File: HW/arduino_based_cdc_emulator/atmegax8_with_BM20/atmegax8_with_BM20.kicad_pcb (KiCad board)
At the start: 2 copper layers, 66 parts, among them IC1 ATMEGA88-A, J1 TEST_FLASH_MODE, P1 CONN_10, P2 SPI, U1 78L05-RESCUE-atmegax8_with_BM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, U2 BM20, U3 LM358, Y1 Crystal_GND24

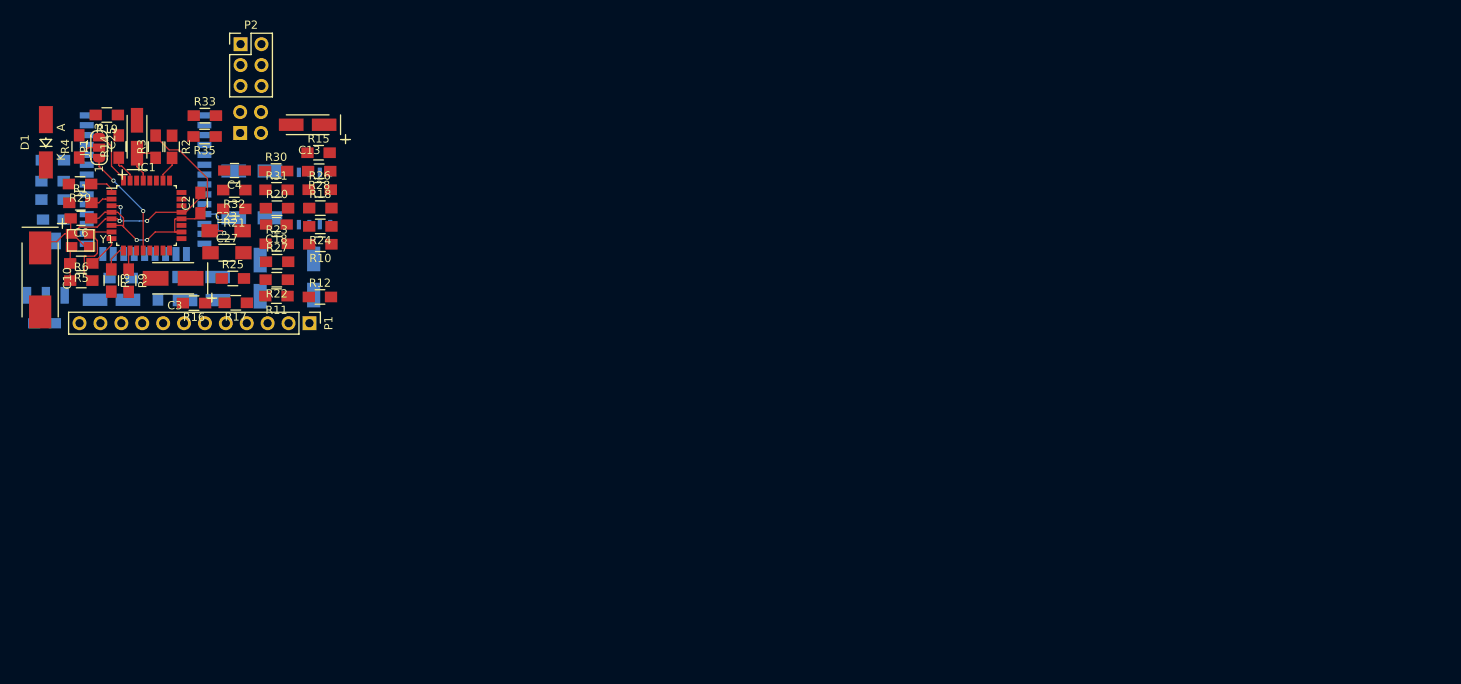
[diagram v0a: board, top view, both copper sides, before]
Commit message: bm20 version update to 328PB
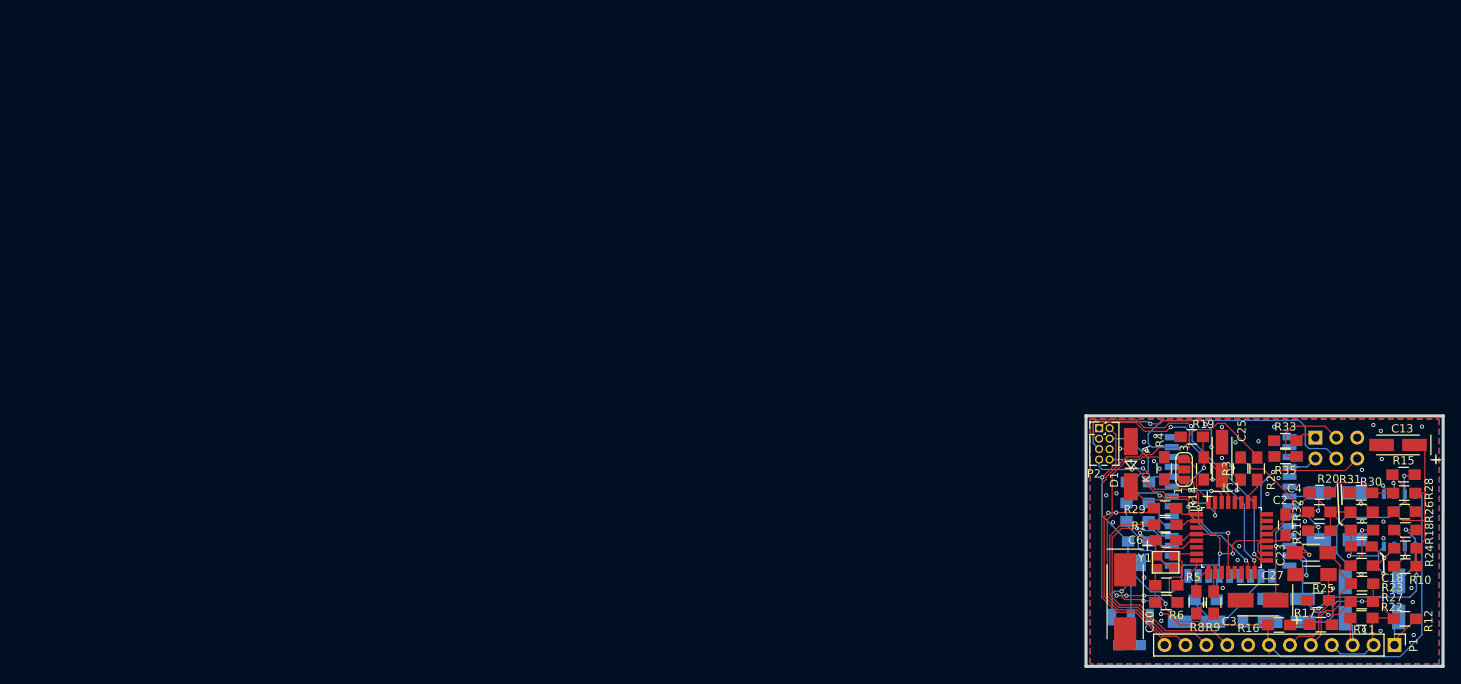
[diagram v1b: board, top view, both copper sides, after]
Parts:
- C14: value 4u7/25V -> 10u/16V
- C9: value 47m/25V -> 10m/16V
- IC1: value ATMEGA88-A -> ATMEGA328PB-AU; footprint Housings_QFP.pretty:LQFP-32_7x7mm_Pitch0.8mm -> Housings_QFP.pretty:TQFP-32_7x7mm_Pitch0.8mm
- J1: footprint Pin_Headers:Pin_Header_Straight_2x02_Pitch2.54mm -> Pin_Headers:Pin_Header_Straight_2x03_Pitch2.54mm
- P2: footprint Pin_Headers:Pin_Header_Straight_2x03_Pitch2.54mm -> Pin_Headers:Pin_Header_Straight_2x04_Pitch1.27mm
- U1: value 78L05-RESCUE-atmegax8_with_BM20 -> 78L05
- moved C13 138.1 mm to (124.1, 85.5)
- moved R29 137.6 mm to (95.8, 93.2)
- moved C1 137.5 mm to (91.5, 109.9)
- moved C10 137.5 mm to (91.0, 104.6)
- moved C14 137.5 mm to (124.2, 104.2)
- moved C2 137.5 mm to (110.5, 95.3)
- moved C21 137.5 mm to (116.7, 97.1)
- moved C22 137.5 mm to (110.5, 104.2)
- moved C23 137.5 mm to (113.6, 98.6)
- moved C24 137.5 mm to (99.7, 107.0)
- moved C25 137.5 mm to (102.8, 87.2)
- moved C27 137.5 mm to (113.7, 101.3)
- moved C28 137.5 mm to (110.6, 107.0)
- moved C4 137.5 mm to (114.6, 91.3)
- moved C5 137.5 mm to (116.7, 91.4)
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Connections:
- IC1 pad 3: GND -> (no net)
- IC1 pad 30: Net-(IC1-Pad30) -> /RX
- IC1 pad 31: Net-(IC1-Pad31) -> /TX
- IC1 pad 6: +5V -> (no net)
- J1 pad 1: /P2_0 -> Net-(J1-Pad1)
- J1 pad 2: /P2_4 -> /P2_0
- J1 pad 4: Net-(J1-Pad4) -> /P2_4
- R13 pad 1: Net-(IC1-Pad30) -> /MOSI
- R13 pad 2: /RX -> /BT_RX
- R14 pad 1: Net-(IC1-Pad31) -> /MISO
- R14 pad 2: /TX -> /BT_TX
- R19 pad 1: /TX -> /BT_TX
- R33 pad 2: Net-(J1-Pad4) -> Net-(J1-Pad1)
- U2 pad 32: /RX -> /BT_TX
- U2 pad 33: /TX -> /BT_RX
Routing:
- net +12V: track 0.00 -> 72.8 mm, vias 0 -> 3
- net Net-(P1-Pad12): track 0.00 -> 49.0 mm
- net +5V: track 34.1 -> 81.0 mm, vias 2 -> 3
- net /VGND: track 0.00 -> 45.0 mm, vias 0 -> 2
- net GNDA: track 0.00 -> 43.6 mm, vias 0 -> 3
- net /BT_RESET: track 0.00 -> 39.4 mm, vias 0 -> 2
- net /DataOut: track 0.00 -> 36.7 mm
- net /SCK: track 0.00 -> 35.8 mm, vias 0 -> 2
- net /MISO: track 0.00 -> 34.1 mm, vias 0 -> 3
- net /MOSI: track 0.00 -> 31.4 mm, vias 0 -> 3
- net /P2_4: track 0.00 -> 31.0 mm
- net /MFB: track 0.00 -> 30.3 mm, vias 0 -> 5
- net Net-(P1-Pad9): track 0.00 -> 30.0 mm
- net /CDC_ENA_12V: track 0.00 -> 28.6 mm, vias 0 -> 2
- net /ARESET: track 6.13 -> 32.1 mm, vias 0 -> 3
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- added copper zone on B.Cu, net GND
- added copper zone on F.Cu, net GND
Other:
- board outline added: 43.4 x 30.4 mm
- board text added: "P2_0 P2_4 BT_RES"

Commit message: disabled input filters,for now
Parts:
- C18, C4: value 10n -> NP
- R20, R31: value 560 -> NP
- R23, R30: value 820 -> 0
- U1: value 78L05 -> 78L05-RESCUE-atmegax8_with_BM20
